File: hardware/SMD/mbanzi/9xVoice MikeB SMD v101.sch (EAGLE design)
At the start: 82 parts, among them IC1 ATMEGA328P, IC2 LE33CZ, IC3 LM386N, IC4 LM7805CT, Q1 12MHz, T1 BSS295, T2 BSS295

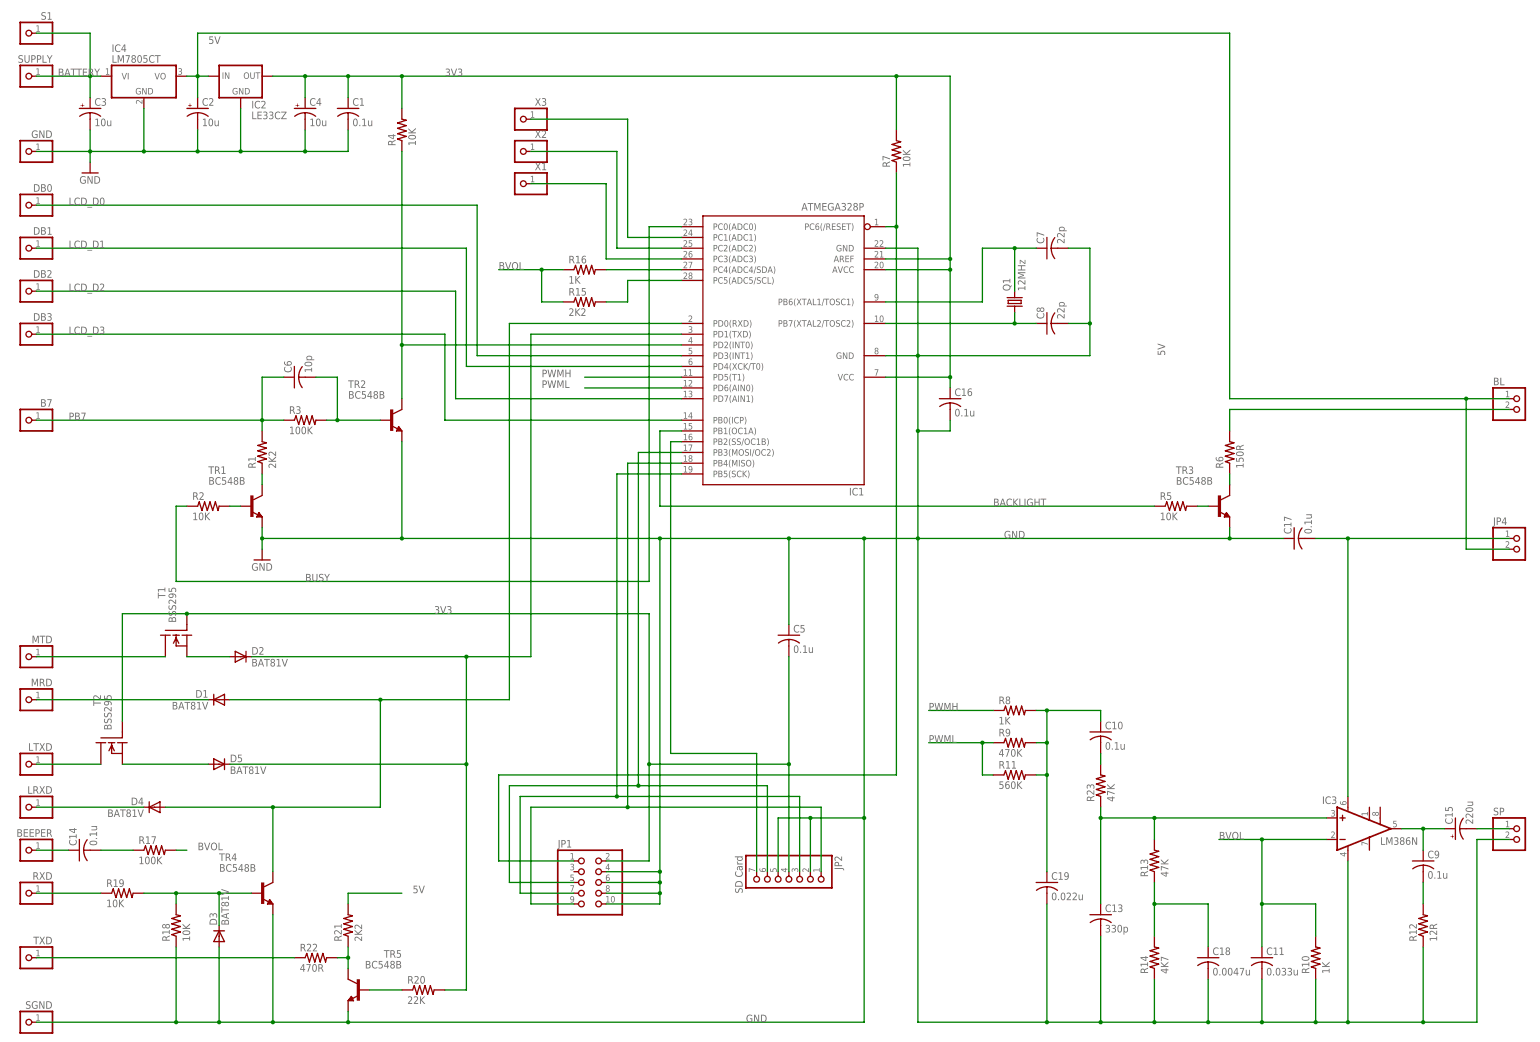
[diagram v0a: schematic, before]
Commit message: Added Eagle 6.3.0 files for all my versions of the designs
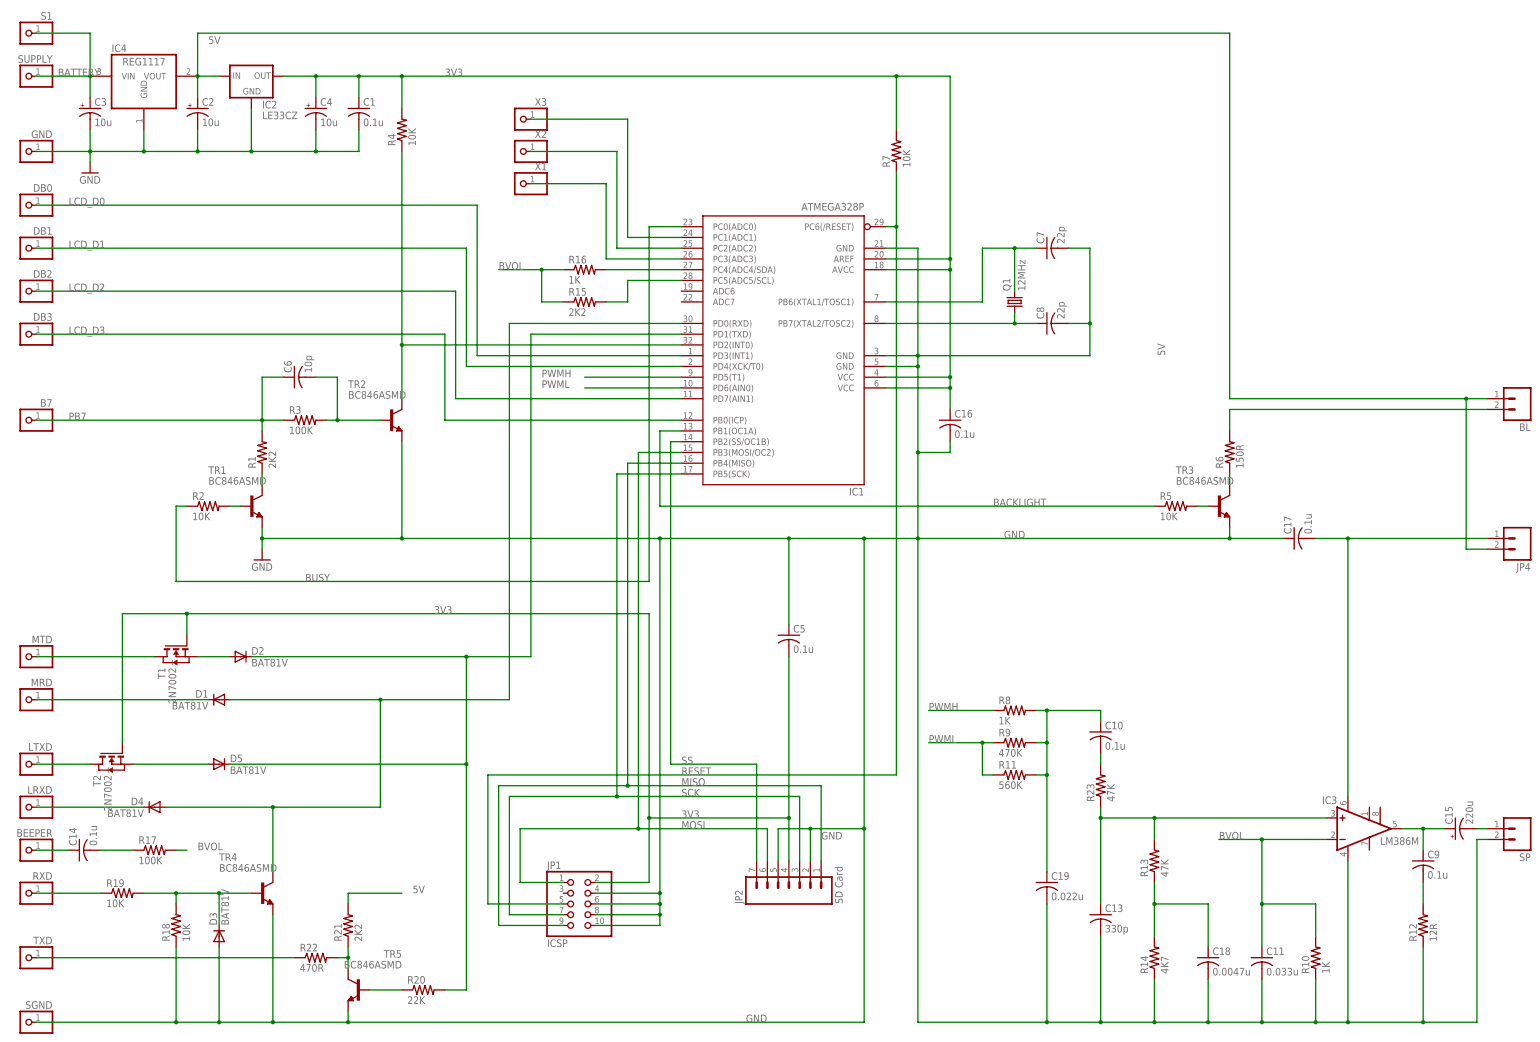
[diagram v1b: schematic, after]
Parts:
- BL, JP4, SP: device pinhead:PINHD-1X2 -> SparkFun-Connectors:M02PTH
- C1, C10, C11, C13, C14, C16, C17, C18, C19, C5, C6, C7, C8, C9: device rcl:C-US025-024X044 -> rcl:C-USC1206
- C15: device rcl:CPOL-USE2.5-7 -> rcl:CPOL-USCT7343
- C2, C3, C4: device rcl:CPOL-USE1.8-4 -> rcl:CPOL-USA/3216-18R
- D1, D2, D3, D4, D5: device diode:DIODE-D-2.5 -> diode:DIODE-SOD123
- IC1: device atmel:MEGA8-P -> atmel:MEGA8-AI; MPN (none) -> ATMEGA8-16AU; OC_FARNELL (none) -> 9171371; OC_NEWARK (none) -> 73M8863
- IC2: device v-reg:78LXX -> v-reg:XC63FPM
- IC3: value LM386N -> LM386M; device linear:LM386N-1 -> linear:LM386M-1
- IC4: value LM7805CT -> REG1117; device linear:7805T -> burr-brown:REG1117
- JP1: value (none) -> ICSP
- JP2: device pinhead:PINHD-1X7 -> SparkFun-Connectors:M07
- Q1: device crystal:CRYSTALHC49S -> jdc:7A
- R1, R10, R11, R12, R13, R14, R15, R16, R17, R18, R19, R20, R21, R22, R23, R3, R4, R5, R6, R7, R8, R9: device rcl:R-US_0207/2V -> rcl:R-US_R1206
- R2: device rcl:R-US_0207/10 -> rcl:R-US_R1206
- T1, T2: value BSS295 -> 2N7002; device transistor-fet:BSS295 -> zetex:NMOSSOT23
- TR1, TR2, TR3, TR4, TR5: value BC548B -> BC846ASMD; device transistor-npn:BC548B -> transistor-npn:BC846ASMD
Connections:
- net 3V3: now also IC1.VCC@2
- net 5V: now also IC4.VOUT; no longer IC4.VO
- net BATTERY: now also IC4.VIN; no longer IC4.VI
- net GND: now also IC1.GND@2
- net MOSI: now also JP1.1; no longer JP1.5
- net RESET: now also JP1.5; no longer JP1.1
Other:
- moved on the sheet: BL, C1, C16, C4, JP1, JP4, SP
